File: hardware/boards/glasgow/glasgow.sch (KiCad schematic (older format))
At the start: 94 parts, among them J1 USB_C_USB2.0, SW1 SW_Push, U1 CY7C68013A-56LTX, U15 TPD3S014, U2 CAT24M01X, U3 BL24C256A-SFRC, U30 ICE40HX8K-BG121, U36 TLV73312PQDRVRQ1, U7 APX811-40UG-7, U8 TLV75533PDRVR, Y1 24M

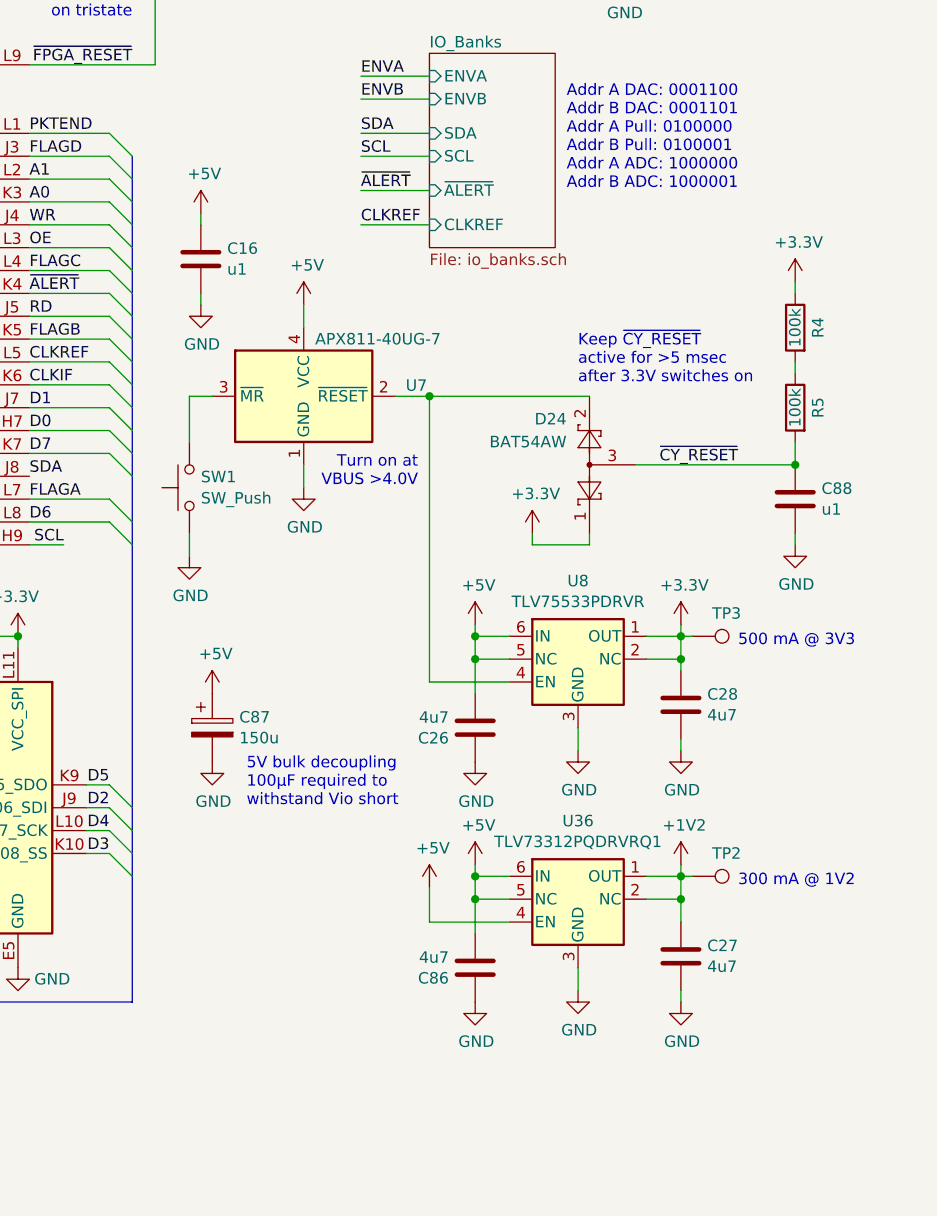
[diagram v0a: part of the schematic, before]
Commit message: revC2: Bigger footprint bulk cap and reset button.
Details:
* Replaced the bulk capacitance polymer capacitor with a larger
footprint version as the 6.3mm footprint is more common.
* Added a reset button that instantly resets the cirucuit. Meant also as
emergency stop. Reset will result in cutting power to the target instantly.
  * To enable reset we replaced the power supervisor chip with one that
  has a reset pin.
  * As the pullup current of the supervisor chip reset line is very low,
  we have added a capacitor parallel to the tact switch, to improve
  "wetting current" and break down contact oxides.
  * To make space for the reset button I decided to replace the SO8
  EEPROMs with TSSOP-8 packaged versions.
* While already moving things arouond I increased the gaps between the
status LEDs from 1.75mm to round 2.00mm. This should make lightpiping
easier when we design a case for the glasgow.
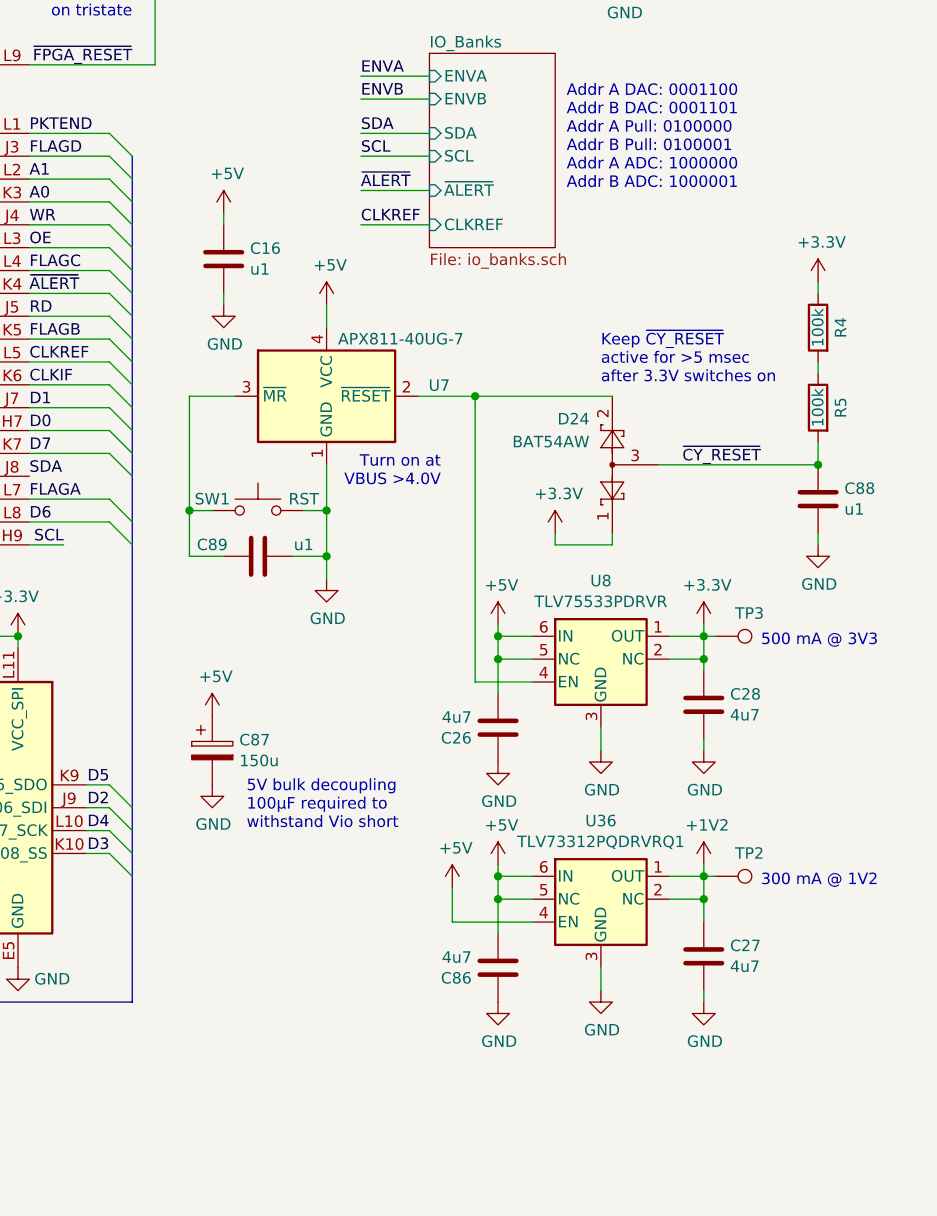
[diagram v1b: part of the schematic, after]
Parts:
- added C89: u1, Capacitor_SMD:C_0402_1005Metric, symbol Device:C
- C87: footprint Capacitor_SMD:CP_Elec_6.3x5.8 -> Capacitor_SMD:CP_Elec_6.3x5.9; 1b2-bom-key cap-poly-5x3_9-150u -> cap-poly-6_3x6_0-10v-150u; Characteristics (none) -> 10V; MPN APXF6R3ARA151ME40G -> A765EB157M1ALAE022; Mfg United Chemi-Con -> KEMET
- SW1: value SW_Push -> RST
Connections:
- net GND: now also C89.2
- net at SW1.2, U7.3 (~MR): now also C89.1
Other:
- moved on the sheet: C16, C26, C27, C28, C86, C87, C88, D24, R4, R5, SW1, TP2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

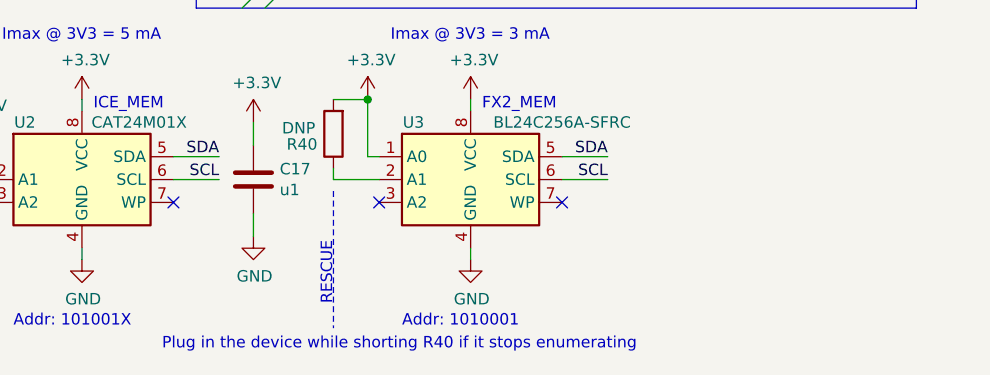
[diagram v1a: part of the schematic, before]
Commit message: revC2: adapt text about recovery in schematics to match current silkscreen + reset button
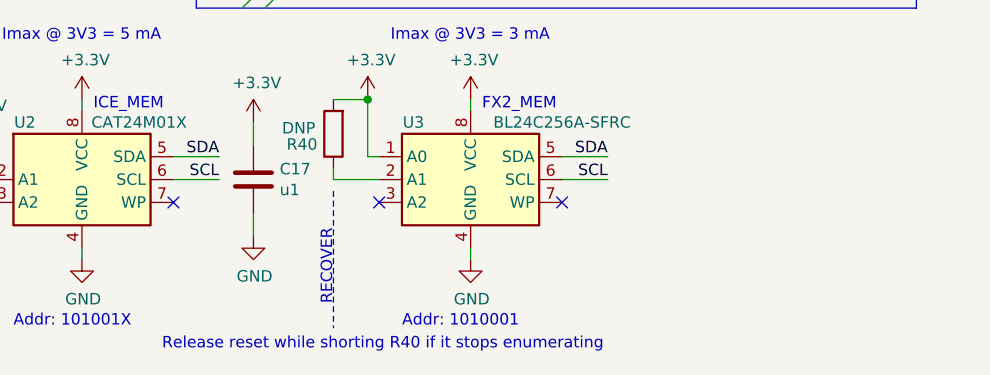
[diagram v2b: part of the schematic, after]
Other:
- note added: "RECOVER"
- note added: "Release reset while shorting R40 if it stops enumerating"
- note removed: "Plug in the device while shorting R40 if it stops enumerating"
- note removed: "RESCUE"
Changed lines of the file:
@@
 	5300 7050 5300 7650
 Text Notes 4550 7750 0    50   ~ 0
-Plug in the device while shorting R40 if it stops enumerating
+Release reset while shorting R40 if it stops enumerating
 NoConn ~ 1500 5450
 NoConn ~ 1500 5550
@@
 	10850 3450 10850 3500
 Text Notes 5300 7550 1    50   ~ 0
-RESCUE
+RECOVER
 $Comp
 L Power_Supervisor:CAT811JTBI-GT3 U7

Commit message: revC2: add bom keys and datasheet for button + reset ic
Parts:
- SW1: 1b2-bom-key (none) -> ???; MPN (none) -> SKRPABE010; Mfg (none) -> Alps Alpine
- U7: 1b2-bom-key (none) -> ic-cat811jtbi; Key ic-cat811jtbi -> (none); MPN (none) -> APX811-40UG-7; Manufacturer Diodes Incorporated -> (none); Mfg (none) -> Diodes Incorporated
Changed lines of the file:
@@
 F 2 "Package_TO_SOT_SMD:SOT-143" H 8800 3300 50  0001 L CNN
 F 3 "https://www.diodes.com/assets/Datasheets/APX811_812.pdf" H 8350 2900 50  0001 C CNN
-F 4 "ic-cat811jtbi" H 8700 3600 50  0001 C CNN "Key"
-F 5 "Diodes Incorporated" H 8700 3600 50  0001 C CNN "Manufacturer"
+F 4 "ic-cat811jtbi" H 8700 3600 50  0001 C CNN "1b2-bom-key"
+F 5 "Diodes Incorporated" H 8700 3600 50  0001 C CNN "Mfg"
+F 6 "APX811-40UG-7" H 8700 3600 50  0001 C CNN "MPN"
 	1    8700 3600
 	1    0    0    -1
@@
 F 1 "RST" H 8200 4150 50  0000 C CNN
 F 2 "Button_Switch_SMD:SW_SPST_PTS810" H 8400 4300 50  0001 C CNN
-F 3 "~" H 8400 4300 50  0001 C CNN
+F 3 "https://tech.alpsalpine.com/prod/e/html/tact/surfacemount/skrp/skrpabe010.html" H 8400 4300 50  0001 C CNN
+F 4 "Alps Alpine" H 8400 4100 50  0001 C CNN "Mfg"
+F 5 "SKRPABE010" H 8400 4100 50  0001 C CNN "MPN"
+F 6 "???" H 8400 4100 50  0001 C CNN "1b2-bom-key"
 	1    8400 4100
 	-1   0    0    -1

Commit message: revC2: Replaced 0603 HandSolder footprints with regular ones.
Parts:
- C1, C14, C19, C26, C27, C28, C76, C80, C86: footprint Capacitor_SMD:C_0603_1608Metric_Pad1.05x0.95mm_HandSolder -> Capacitor_SMD:C_0603_1608Metric
- D1, D2, D3, D4, D5: footprint LED_SMD:LED_0603_1608Metric_Pad1.05x0.95mm_HandSolder -> LED_SMD:LED_0603_1608Metric
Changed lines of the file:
@@
 F 0 "C1" H 1115 1196 50  0000 L CNN
 F 1 "4u7" H 1115 1105 50  0000 L CNN
-F 2 "Capacitor_SMD:C_0603_1608Metric_Pad1.05x0.95mm_HandSolder" H 1038 1000 50  0001 C CNN
+F 2 "Capacitor_SMD:C_0603_1608Metric" H 1038 1000 50  0001 C CNN
 F 3 "https://www.mouser.com/datasheet/2/400/lcc_commercial_general_en-837201.pdf" H 1000 1150 50  0001 C CNN
 F 4 "Taiyo Yuden" H -450 -250 50  0001 C CNN "Mfg"
@@
 F 0 "C19" H 5265 1196 50  0000 L CNN
 F 1 "4u7" H 5265 1105 50  0000 L CNN
-F 2 "Capacitor_SMD:C_0603_1608Metric_Pad1.05x0.95mm_HandSolder" H 5188 1000 50  0001 C CNN
+F 2 "Capacitor_SMD:C_0603_1608Metric" H 5188 1000 50  0001 C CNN
 F 3 "https://www.mouser.com/datasheet/2/400/lcc_commercial_general_en-837201.pdf" H 5150 1150 50  0001 C CNN
 F 4 "Taiyo Yuden" H 450 -250 50  0001 C CNN "Mfg"
@@
 F 0 "C26" H 9565 5096 50  0000 L CNN
 F 1 "4u7" H 9565 5005 50  0000 L CNN
-F 2 "Capacitor_SMD:C_0603_1608Metric_Pad1.05x0.95mm_HandSolder" H 9488 4900 50  0001 C CNN
+F 2 "Capacitor_SMD:C_0603_1608Metric" H 9488 4900 50  0001 C CNN
 F 3 "https://www.mouser.com/datasheet/2/400/lcc_commercial_general_en-837201.pdf" H 9450 5050 50  0001 C CNN
 F 4 "Taiyo Yuden" H 0   -1000 50  0001 C CNN "Mfg"
@@
 F 0 "C27" H 10465 6096 50  0000 L CNN
 F 1 "4u7" H 10465 6005 50  0000 L CNN
-F 2 "Capacitor_SMD:C_0603_1608Metric_Pad1.05x0.95mm_HandSolder" H 10388 5900 50  0001 C CNN
+F 2 "Capacitor_SMD:C_0603_1608Metric" H 10388 5900 50  0001 C CNN
 F 3 "https://www.mouser.com/datasheet/2/400/lcc_commercial_general_en-837201.pdf" H 10350 6050 50  0001 C CNN
 F 4 "Taiyo Yuden" H -50 0   50  0001 C CNN "Mfg"
@@
 F 0 "C28" H 10465 4996 50  0000 L CNN
 F 1 "4u7" H 10465 4905 50  0000 L CNN
-F 2 "Capacitor_SMD:C_0603_1608Metric_Pad1.05x0.95mm_HandSolder" H 10388 4800 50  0001 C CNN
+F 2 "Capacitor_SMD:C_0603_1608Metric" H 10388 4800 50  0001 C CNN
 F 3 "https://www.mouser.com/datasheet/2/400/lcc_commercial_general_en-837201.pdf" H 10350 4950 50  0001 C CNN
 F 4 "Taiyo Yuden" H -450 -1100 50  0001 C CNN "Mfg"
@@
 F 0 "D1" H 9500 900 50  0000 C CNN
 F 1 "GRN" H 9350 900 50  0000 C CNN
-F 2 "LED_SMD:LED_0603_1608Metric_Pad1.05x0.95mm_HandSolder" H 9800 900 50  0001 C CNN
+F 2 "LED_SMD:LED_0603_1608Metric" H 9800 900 50  0001 C CNN
 F 3 "https://www.mouser.com/datasheet/2/445/150060GS75000-368921.pdf" H 9800 900 50  0001 C CNN
 F 4 "Wurth Electronics" H -450 0   50  0001 C CNN "Mfg"
@@
 F 0 "D2" H 9500 1100 50  0000 C CNN
 F 1 "GRN" H 9350 1100 50  0000 C CNN
-F 2 "LED_SMD:LED_0603_1608Metric_Pad1.05x0.95mm_HandSolder" H 9800 1100 50  0001 C CNN
+F 2 "LED_SMD:LED_0603_1608Metric" H 9800 1100 50  0001 C CNN
 F 3 "https://www.mouser.com/datasheet/2/445/150060GS75000-368921.pdf" H 9800 1100 50  0001 C CNN
 F 4 "Wurth Electronics" H -450 0   50  0001 C CNN "Mfg"
@@
 F 0 "D3" H 9500 1300 50  0000 C CNN
 F 1 "GRN" H 9350 1300 50  0000 C CNN
-F 2 "LED_SMD:LED_0603_1608Metric_Pad1.05x0.95mm_HandSolder" H 9800 1300 50  0001 C CNN
+F 2 "LED_SMD:LED_0603_1608Metric" H 9800 1300 50  0001 C CNN
 F 3 "https://www.mouser.com/datasheet/2/445/150060GS75000-368921.pdf" H 9800 1300 50  0001 C CNN
 F 4 "Wurth Electronics" H -450 0   50  0001 C CNN "Mfg"
@@
 F 0 "D4" H 9500 1500 50  0000 C CNN
 F 1 "YEL" H 9350 1500 50  0000 C CNN
-F 2 "LED_SMD:LED_0603_1608Metric_Pad1.05x0.95mm_HandSolder" H 9800 1500 50  0001 C CNN
+F 2 "LED_SMD:LED_0603_1608Metric" H 9800 1500 50  0001 C CNN
 F 3 "https://www.mouser.com/datasheet/2/445/150060YS75000-368983.pdf" H 9800 1500 50  0001 C CNN
 F 4 "Wurth Electronics" H -450 0   50  0001 C CNN "Mfg"
@@
 F 0 "D5" H 9500 1700 50  0000 C CNN
 F 1 "RED" H 9350 1700 50  0000 C CNN
-F 2 "LED_SMD:LED_0603_1608Metric_Pad1.05x0.95mm_HandSolder" H 9800 1700 50  0001 C CNN
+F 2 "LED_SMD:LED_0603_1608Metric" H 9800 1700 50  0001 C CNN
 F 3 "https://www.mouser.com/datasheet/2/445/150060RS75000-368563.pdf" H 9800 1700 50  0001 C CNN
 F 4 "Wurth Electronics" H -450 0   50  0001 C CNN "Mfg"
@@
 F 0 "C80" H 6115 5696 50  0000 L CNN
 F 1 "4u7" H 6115 5605 50  0000 L CNN
-F 2 "Capacitor_SMD:C_0603_1608Metric_Pad1.05x0.95mm_HandSolder" H 6038 5500 50  0001 C CNN
+F 2 "Capacitor_SMD:C_0603_1608Metric" H 6038 5500 50  0001 C CNN
 F 3 "https://www.mouser.com/datasheet/2/400/lcc_commercial_general_en-837201.pdf" H 6000 5650 50  0001 C CNN
 F 4 "Taiyo Yuden" H -1600 4100 50  0001 C CNN "Mfg"
@@
 F 0 "C14" H 7115 1196 50  0000 L CNN
 F 1 "4u7" H 7115 1105 50  0000 L CNN
-F 2 "Capacitor_SMD:C_0603_1608Metric_Pad1.05x0.95mm_HandSolder" H 7038 1000 50  0001 C CNN
+F 2 "Capacitor_SMD:C_0603_1608Metric" H 7038 1000 50  0001 C CNN
 F 3 "https://www.mouser.com/datasheet/2/400/lcc_commercial_general_en-837201.pdf" H 7000 1150 50  0001 C CNN
 F 4 "Taiyo Yuden" H 5550 -250 50  0001 C CNN "Mfg"
@@
 F 0 "C76" H 6115 5296 50  0000 L CNN
 F 1 "4u7" H 6115 5205 50  0000 L CNN
-F 2 "Capacitor_SMD:C_0603_1608Metric_Pad1.05x0.95mm_HandSolder" H 6038 5100 50  0001 C CNN
+F 2 "Capacitor_SMD:C_0603_1608Metric" H 6038 5100 50  0001 C CNN
 F 3 "https://www.mouser.com/datasheet/2/400/lcc_commercial_general_en-837201.pdf" H 6000 5250 50  0001 C CNN
 F 4 "Taiyo Yuden" H -1600 3700 50  0001 C CNN "Mfg"
@@
 F 0 "C86" H 9565 6146 50  0000 L CNN
 F 1 "4u7" H 9565 6055 50  0000 L CNN
-F 2 "Capacitor_SMD:C_0603_1608Metric_Pad1.05x0.95mm_HandSolder" H 9488 5950 50  0001 C CNN
+F 2 "Capacitor_SMD:C_0603_1608Metric" H 9488 5950 50  0001 C CNN
 F 3 "https://www.mouser.com/datasheet/2/400/lcc_commercial_general_en-837201.pdf" H 9450 6100 50  0001 C CNN
 F 4 "Taiyo Yuden" H 0   50  50  0001 C CNN "Mfg"

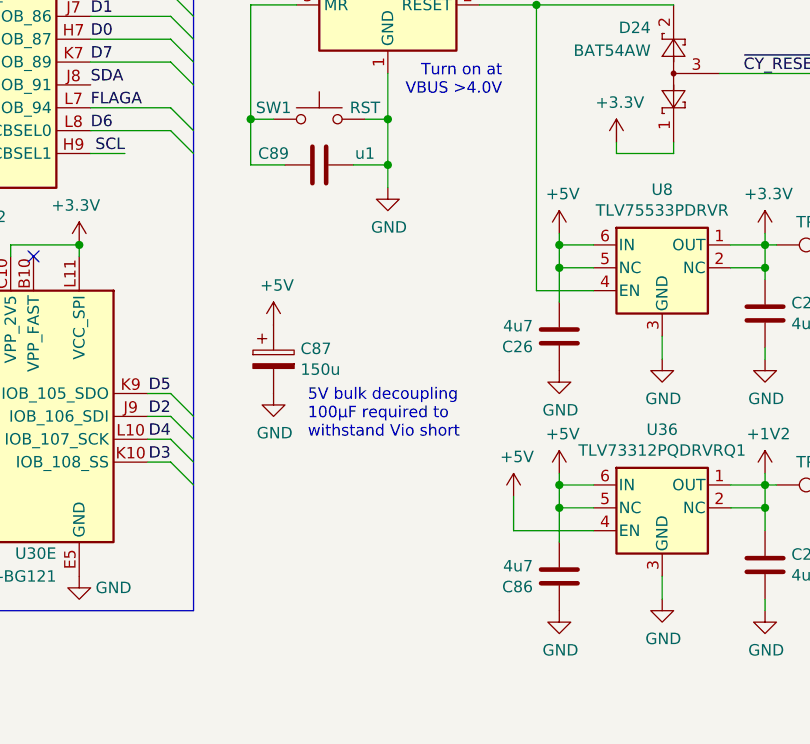
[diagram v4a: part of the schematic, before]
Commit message: revC2: add some more documentation about reset to the schematics
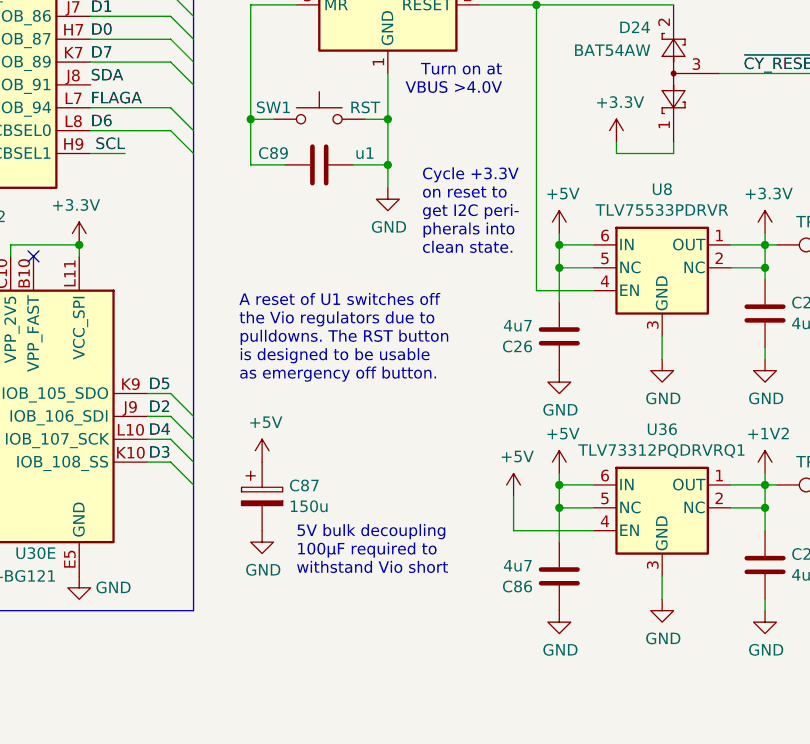
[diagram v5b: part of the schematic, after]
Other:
- note added: "A reset of U1 switches off \nthe Vio regulators due to \npulldowns. The RST button\nis designed to be usable \nas emergency off button."
- note added: "Cycle +3.3V\non reset to \nget I2C peri-\npherals into \nclean state."
- moved on the sheet: C87
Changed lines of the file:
@@
 L power:+5V #PWR0149
 U 1 1 5CCEA64E
-P 8200 5000
-F 0 "#PWR0149" H 8200 4850 50  0001 C CNN
-F 1 "+5V" H 8215 5173 50  0000 C CNN
-F 2 "" H 8200 5000 50  0001 C CNN
-F 3 "" H 8200 5000 50  0001 C CNN
-	1    8200 5000
+P 8150 5600
+F 0 "#PWR0149" H 8150 5450 50  0001 C CNN
+F 1 "+5V" H 8165 5773 50  0000 C CNN
+F 2 "" H 8150 5600 50  0001 C CNN
+F 3 "" H 8150 5600 50  0001 C CNN
+	1    8150 5600
 	1    0    0    -1
 $EndComp
@@
 L power:GND #PWR0150
 U 1 1 5CCEA988
-P 8200 5300
-F 0 "#PWR0150" H 8200 5050 50  0001 C CNN
-F 1 "GND" H 8205 5127 50  0000 C CNN
-F 2 "" H 8200 5300 50  0001 C CNN
-F 3 "" H 8200 5300 50  0001 C CNN
-	1    8200 5300
+P 8150 5900
+F 0 "#PWR0150" H 8150 5650 50  0001 C CNN
+F 1 "GND" H 8155 5727 50  0000 C CNN
+F 2 "" H 8150 5900 50  0001 C CNN
+F 3 "" H 8150 5900 50  0001 C CNN
+	1    8150 5900
 	1    0    0    -1
 $EndComp
@@
 L Device:CP C87
 U 1 1 5CCE6160
-P 8200 5150
-F 0 "C87" H 8318 5196 50  0000 L CNN
-F 1 "150u" H 8318 5105 50  0000 L CNN
-F 2 "Capacitor_SMD:CP_Elec_6.3x5.9" H 8238 5000 50  0001 C CNN
-F 3 "https://api.kemet.com/component-edge/download/datasheet/A765EB157M1ALAE022.pdf" H 8200 5150 50  0001 C CNN
-F 4 "A765EB157M1ALAE022" H 8200 5150 50  0001 C CNN "MPN"
-F 5 "KEMET" H 8200 5150 50  0001 C CNN "Mfg"
-F 6 "cap-poly-6_3x6_0-10v-150u" H 8200 5150 50  0001 C CNN "1b2-bom-key"
-F 7 "10V" H 8200 5150 50  0001 C CNN "Characteristics"
-	1    8200 5150
-	1    0    0    -1
-$EndComp
-Text Notes 8350 5500 0    50   ~ 0
+P 8150 5750
+F 0 "C87" H 8268 5796 50  0000 L CNN
+F 1 "150u" H 8268 5705 50  0000 L CNN
+F 2 "Capacitor_SMD:CP_Elec_6.3x5.9" H 8188 5600 50  0001 C CNN
+F 3 "https://api.kemet.com/component-edge/download/datasheet/A765EB157M1ALAE022.pdf" H 8150 5750 50  0001 C CNN
+F 4 "A765EB157M1ALAE022" H 8150 5750 50  0001 C CNN "MPN"
+F 5 "KEMET" H 8150 5750 50  0001 C CNN "Mfg"
+F 6 "cap-poly-6_3x6_0-10v-150u" H 8150 5750 50  0001 C CNN "1b2-bom-key"
+F 7 "10V" H 8150 5750 50  0001 C CNN "Characteristics"
+	1    8150 5750
+	1    0    0    -1
+$EndComp
+Text Notes 8300 6100 0    50   ~ 0
 5V bulk decoupling\n100µF required to\nwithstand Vio short
 Wire Wire Line
@@
 Wire Bus Line
 	4700 2150 4700 6250
+Text Notes 8050 5250 0    50   ~ 0
+A reset of U1 switches off \nthe Vio regulators due to \npulldowns. The RST button\nis designed to be usable \nas emergency off button.
+Text Notes 8850 4700 0    50   ~ 0
+Cycle +3.3V\non reset to \nget I2C peri-\npherals into \nclean state.
 $EndSCHEMATC

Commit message: revC2: Replaced top actuated tact switch with a side actuated one.
This should make the case design better. This is not necessarily the
final tact switch selection.
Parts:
- SW1: footprint Button_Switch_SMD:SW_SPST_PTS810 -> Glasgow:SW_Tactile_SPST_Angled_1TS003A; MPN SKRPABE010 -> 1TS003A-1600-3500A-CT; Mfg Alps Alpine -> HYP (Hongyuan Precision)
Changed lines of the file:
@@
 F 0 "SW1" H 8600 4150 50  0000 C CNN
 F 1 "RST" H 8200 4150 50  0000 C CNN
-F 2 "Button_Switch_SMD:SW_SPST_PTS810" H 8400 4300 50  0001 C CNN
-F 3 "https://tech.alpsalpine.com/prod/e/html/tact/surfacemount/skrp/skrpabe010.html" H 8400 4300 50  0001 C CNN
-F 4 "Alps Alpine" H 8400 4100 50  0001 C CNN "Mfg"
-F 5 "SKRPABE010" H 8400 4100 50  0001 C CNN "MPN"
+F 2 "Glasgow:SW_Tactile_SPST_Angled_1TS003A" H 8400 4300 50  0001 C CNN
+F 3 "https://datasheet.lcsc.com/szlcsc/1811011023_HYP-Hongyuan-Precision-1TS003A-1600-3500A-CT_C255805.pdf" H 8400 4300 50  0001 C CNN
+F 4 "HYP (Hongyuan Precision)" H 8400 4100 50  0001 C CNN "Mfg"
+F 5 "1TS003A-1600-3500A-CT" H 8400 4100 50  0001 C CNN "MPN"
 F 6 "???" H 8400 4100 50  0001 C CNN "1b2-bom-key"
 	1    8400 4100
@@
 Wire Wire Line
 	8100 4100 8100 4300
+Text Notes 8050 5250 0    50   ~ 0
+A reset of U1 switches off \nthe Vio regulators due to \npulldowns. The RST button\nis designed to be usable \nas emergency off button.
+Text Notes 8850 4700 0    50   ~ 0
+Cycle +3.3V\non reset to \nget I2C peri-\npherals into \nclean state.
 Wire Bus Line
 	4700 6250 7850 6250
@@
 Wire Bus Line
 	4700 2150 4700 6250
-Text Notes 8050 5250 0    50   ~ 0
-A reset of U1 switches off \nthe Vio regulators due to \npulldowns. The RST button\nis designed to be usable \nas emergency off button.
-Text Notes 8850 4700 0    50   ~ 0
-Cycle +3.3V\non reset to \nget I2C peri-\npherals into \nclean state.
 $EndSCHEMATC
